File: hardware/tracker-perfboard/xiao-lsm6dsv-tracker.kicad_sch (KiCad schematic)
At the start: 0 parts

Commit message: XIAO+LSM6DSVトラッカーの回路図をKiCADで作成
hardware/tracker-perfboard/ に8ネットの回路図を作成した。U1(XIAO
ESP32-S3)とU2(LSM6DSVモジュール)は標準ライブラリに無いので
tracker-perfboard.kicad_sym に自作し、${KIPRJMOD} 相対のプロジェクト
スコープで登録している。

Konnectの配置系ツールは sym-lib-table を参照せず組み込みライブラリしか
解決しないため、U1とU2はKiCAD GUIで手配置した。配線・no-connect・ERC・
SVG出力はツール経由。

kicad-cli で独立に検証した。ERC 0件、ネットリストは仕様の8ネットと一致、
単独ピン15本はno-connectフラグと一致。パーフボード実装なのでフットプリント
は割り当てず、.kicad_pcb は触っていない。

Co-Authored-By: Claude Opus 5 <noreply@anthropic.com>
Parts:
- added BT1: Protected 1S Li-ion, symbol Device:Battery_Cell
- added R1: 10k, symbol Device:R
- added R2, R3: 100k, symbol Device:R
- added SW1: SW_Push, symbol Switch:SW_Push
- added U1: Seeed XIAO ESP32-S3, symbol tracker-perfboard:XIAO_ESP32S3
- added U2: LSM6DSV module (BOOTH 5265159A-P1-241122), symbol tracker-perfboard:LSM6DSV_Module
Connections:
- new net +3V3: R1.1, U1.12 (3V3), U2.1 (3V3)
- new net BAT+: BT1.1 (+), R2.1, U1.15 (BAT+)
- new net BAT_SENSE: R2.2, R3.1, U1.1 (D0_GPIO1)
- new net GND: BT1.2 (-), R3.2, SW1.2, U1.13 (GND), U2.2 (GND)
- new net IMU_INT1: U1.11 (D10_GPIO9), U2.5 (INT1)
- new net PWR_BTN: R1.2, SW1.1, U1.9 (D8_GPIO7)
- new net SCL: U1.6 (D5_GPIO6), U2.4 (SCL)
- new net SDA: U1.5 (D4_GPIO5), U2.3 (SDA)
- no-connect marks 0 -> 15

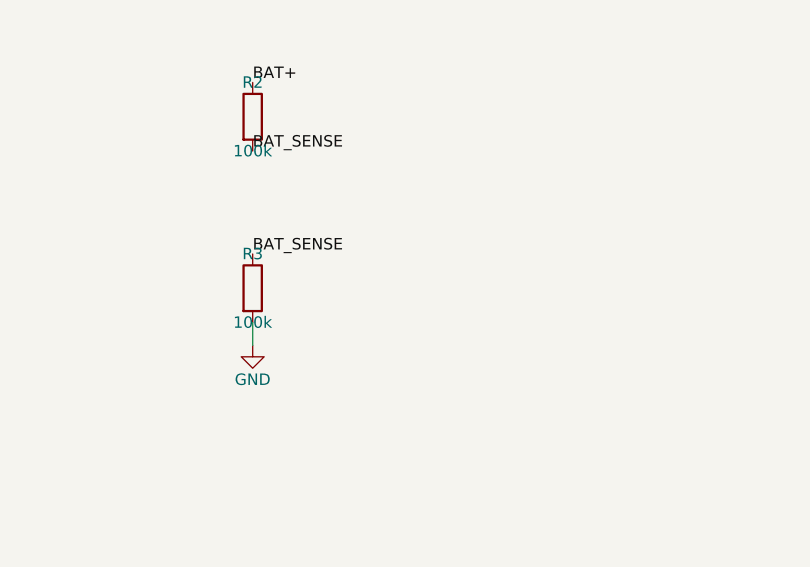
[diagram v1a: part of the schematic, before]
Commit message: C1を実装し回路図と文書を実物に合わせた
100nF 50V の積層セラミックコンデンサをR3と並列、BAT_SENSEノードと
GNDの間に実装した。2026-08-04の「C1は実装しない」という決定を
上書きする。分圧比は変わらないためADCMultiplierは2のままで、
ファームウェアの変更は不要。時定数は約5ms、アイドル電流は約21uA
のまま。

C1が担うのは、ADCのサンプル&ホールドが約50kOhmの高インピーダンス
源から電荷を引く際の供給。これを見越して入れてあった中央値
フィルタ(BATTERY_ADC_SAMPLES=15)は無効化していない。同じ問題への
対策であり併用した方が良いため。

回路図はKonnect MCP経由の子claudeプロセスで編集した。子は
エクスポートしたネットリストの読み取り権限がなく自己検証できずに
終了したため、kicad-cliで独立に検証した:
- sch erc --severity-all: Found 0 violations
- ネットリスト: C1.1がBAT_SENSE(C1.1,R2.2,R3.1,U1.1)、C1.2が
  GND(BT1.2,C1.2,R3.2,SW1.2,U1.13,U2.2)。他6ネットと15個の
  未接続フラグに変化なし
部品点数は7から8になった(SW2は引き続き不在)。SVGも再出力した。

.gitattributesを新規追加した。kicad-cliのSVG出力は行末空白を多数
含み(既存コミット済みファイルにも577行)、AGENTS.mdが要求する
git diff --checkが図面の再出力ごとに必ず失敗してしまうため、
*.svgを対象外にした。手書きコードの検出という本来の役割を保つ
ための措置。

バッテリ分圧の校正については、オーナー判断により実施しないことと
した。残量は粗い指標として扱う。

Co-Authored-By: Claude Opus 5 <noreply@anthropic.com>
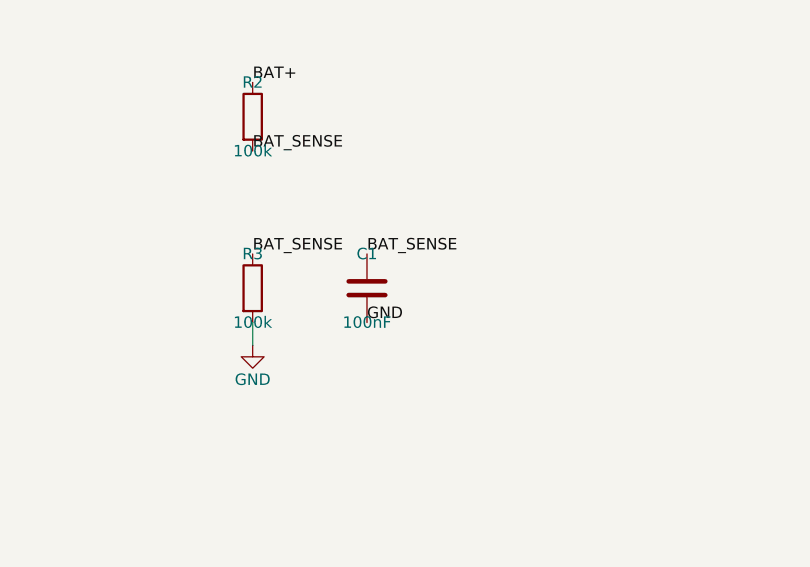
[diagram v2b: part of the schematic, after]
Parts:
- added C1: 100nF, symbol Device:C
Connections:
- net BAT_SENSE: now also C1.1
- net GND: now also C1.2
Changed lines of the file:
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@@
+      (justify left bottom))
+)
+  (label "BAT_SENSE"
+    (at 180.34 129.54 0)
+    (effects
+      (font
+        (size 1.27 1.27))
+      (justify left bottom))
+)
+  (label "GND"
+    (at 180.34 137.16 0)
+    (effects
+      (font
+        (size 1.27 1.27))
       (justify left bottom))
 )
@@
           (reference "#PWR011")
           (unit 1)))))
+  (symbol
+    (lib_id "Device:C")
+    (at 180.34 133.35 0)
+    (unit 1)
+    (in_bom yes)
+    (on_board yes)
+    (dnp no)
+    (property "Reference" "C1"
+      (at 180.34 129.54 0)
+      (effects
+        (font
+          (size 1.27 1.27))))
+    (property "Value" "100nF"
+      (at 180.34 137.16 0)
+      (effects
+        (font
+          (size 1.27 1.27))))
+    (property "Footprint" ""
+      (at 180.34 133.35 0)
+      (hide yes)
+      (effects
+        (font
+          (size 1.27 1.27))))
+    (property "Datasheet" ""
+      (at 180.34 133.35 0)
+      (hide yes)
+      (effects
+        (font
+          (size 1.27 1.27))))
+    (instances
+      (project "xiao-lsm6dsv-tracker"
+        (path "/c885719e-373f-4494-a55a-577bf25c909c"
+          (reference "C1")
+          (unit 1)))))
   (embedded_fonts no)
